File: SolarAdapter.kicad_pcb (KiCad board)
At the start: 2 copper layers, 32.4 x 18 mm, 7 parts, among them J1 Conn_02x03_Odd_Even, J2 USB_A

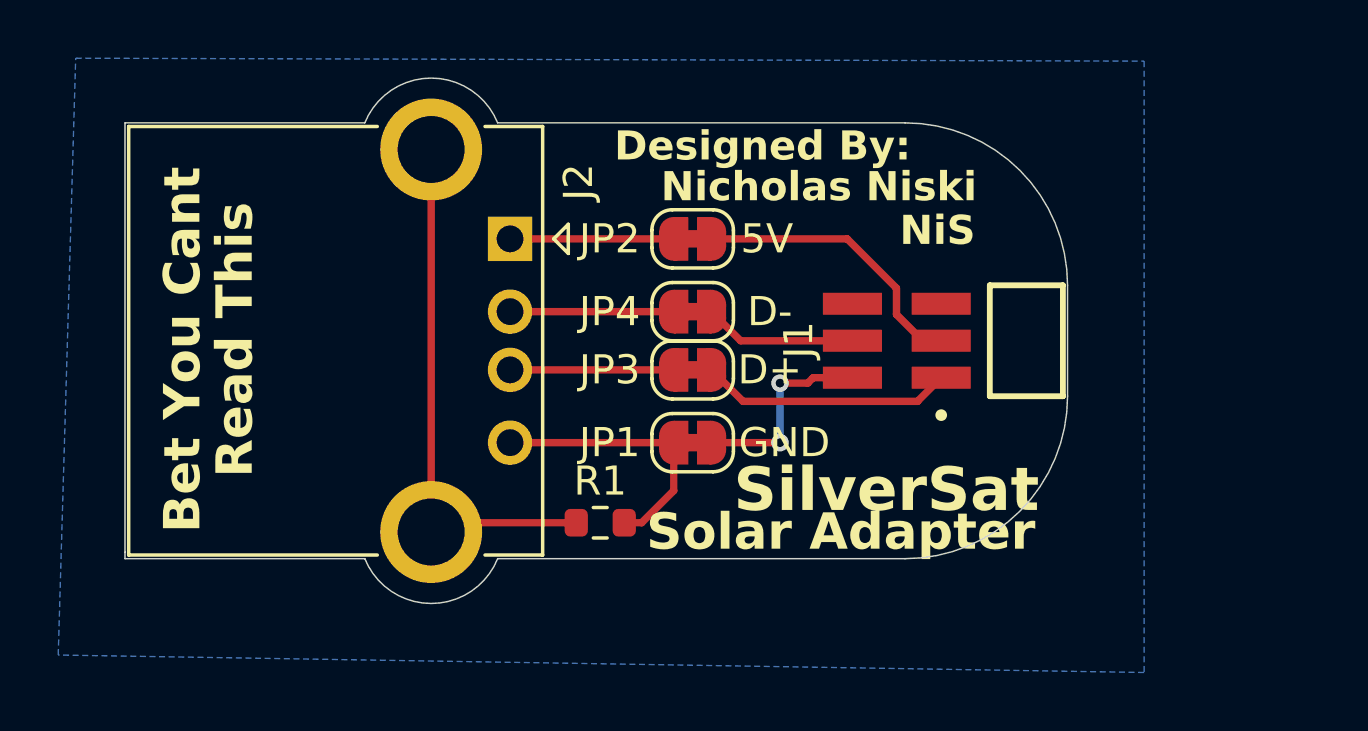
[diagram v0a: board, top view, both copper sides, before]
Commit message: Solar Adapter 1.1
Release Notes:
1. Added MPNs to parts(whoops)
2. Beefed up power traces to allow for higher current draws
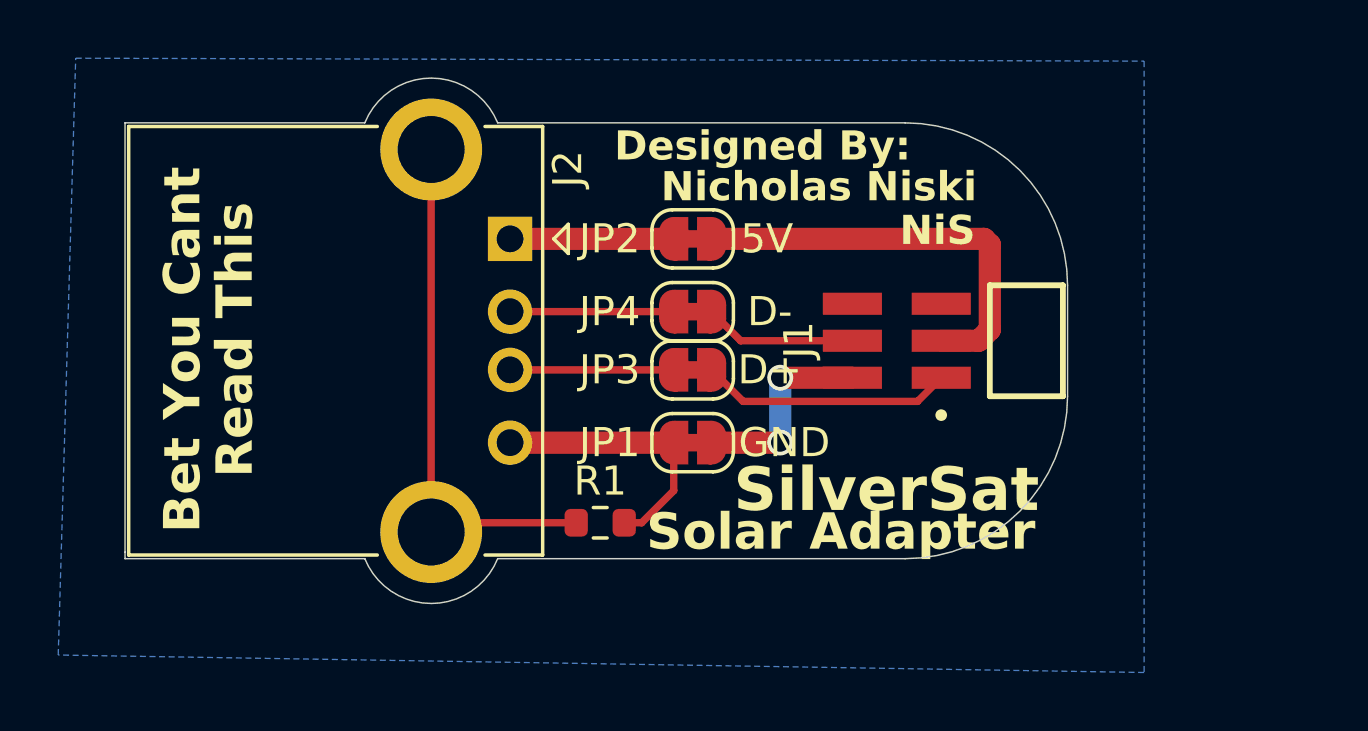
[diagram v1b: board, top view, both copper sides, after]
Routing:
- net /CVBUS: track 9.87 -> 15.0 mm
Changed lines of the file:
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@@
 		(sheetfile "SolarAdapter.kicad_sch")
 		(zone_connect 1)
-		(attr exclude_from_pos_files)
+		(attr exclude_from_pos_files exclude_from_bom)
 		(net_tie_pad_groups "1, 2")
 		(fp_poly
@@
 		(sheetfile "SolarAdapter.kicad_sch")
 		(zone_connect 1)
-		(attr exclude_from_pos_files)
+		(attr exclude_from_pos_files exclude_from_bom)
 		(net_tie_pad_groups "1, 2")
 		(fp_poly
@@
 		(tags "USB-A receptacle horizontal through-hole")
 		(property "Reference" "J2"
-			(at -1.95 -2.35 90)
+			(at -2.405 -1.98 90)
 			(layer "F.SilkS")
 			(effects
@@
 				(font
 					(size 1.27 1.27)
+				)
+			)
+		)
+		(property "MPN" "6364372-2"
+			(at 0 0 -90)
+			(unlocked yes)
+			(layer "F.Fab")
+			(hide yes)
+			(effects
+				(font
+					(size 1 1)
+					(thickness 0.15)
 				)
 			)
@@
 		(sheetfile "SolarAdapter.kicad_sch")
 		(zone_connect 1)
-		(attr exclude_from_pos_files)
+		(attr exclude_from_pos_files exclude_from_bom)
 		(net_tie_pad_groups "1, 2")
 		(fp_poly
@@
 			)
 		)
+		(property "MPN" "FTSH-103-04-L-DH"
+			(at 0 0 -90)
+			(unlocked yes)
+			(layer "F.Fab")
+			(hide yes)
+			(effects
+				(font
+					(size 1 1)
+					(thickness 0.15)
+				)
+			)
+		)
 		(property ki_fp_filters "Connector*:*_2x??_*")
 		(sheetname "Root")
@@
 			)
 		)
+		(property "MPN" "ERJ-PA3F1004V"
+			(at 0 0 0)
+			(unlocked yes)
+			(layer "F.Fab")
+			(hide yes)
+			(effects
+				(font
+					(size 1 1)
+					(thickness 0.15)
+				)
+			)
+		)
 		(property ki_fp_filters "R_*")
 		(sheetname "Root")
@@
 		(sheetfile "SolarAdapter.kicad_sch")
 		(zone_connect 1)
-		(attr exclude_from_pos_files)
+		(attr exclude_from_pos_files exclude_from_bom)
 		(net_tie_pad_groups "1, 2")
 		(fp_poly
@@
 		(start 103.7275 78.5)
 		(end 109.35 78.5)
-		(width 0.254)
+		(width 0.762)
 		(layer "F.Cu")
 		(net 3)
@@
 	)
 	(segment
-		(start 103.7275 85.5)
-		(end 109.35 85.5)
+		(start 107.65 88.25125)
+		(end 108.24875 88.25125)
 		(width 0.254)
 		(layer "F.Cu")
@@
 	)
 	(segment
-		(start 107.65 88.25125)
-		(end 108.24875 88.25125)
-		(width 0.254)
+		(start 103.7275 85.5)
+		(end 109.35 85.5)
+		(width 0.762)
 		(layer "F.Cu")
 		(net 4)
@@
 	)
 	(segment
-		(start 113 83.455)
-		(end 113.955 83.455)
-		(width 0.254)
+		(start 113.0025 85.5)
+		(end 113.0075 85.495)
+		(width 0.762)
 		(layer "F.Cu")
 		(net 6)
 	)
 	(segment
-		(start 114.14 83.27)
+		(start 113.0075 83.27)
 		(end 115.4875 83.27)
-		(width 0.254)
+		(width 0.762)
 		(layer "F.Cu")
 		(net 6)
@@
 	(segment
 		(start 110.65 85.5)
-		(end 113 85.5)
-		(width 0.254)
+		(end 113.0025 85.5)
+		(width 0.762)
 		(layer "F.Cu")
 		(net 6)
 	)
-	(segment
-		(start 113.955 83.455)
-		(end 114.14 83.27)
-		(width 0.254)
-		(layer "F.Cu")
-		(net 6)
-	)
 	(via
-		(at 113 85.5)
-		(size 0.6)
-		(drill 0.3)
+		(at 113.0075 83.27)
+		(size 0.889)
+		(drill 0.635)
 		(layers "F.Cu" "B.Cu")
 		(net 6)
 	)
 	(via
-		(at 113 83.455)
-		(size 0.6)
-		(drill 0.3)
+		(at 113.0075 85.495)
+		(size 0.889)
+		(drill 0.635)
 		(layers "F.Cu" "B.Cu")
 		(net 6)
 	)
 	(segment
-		(start 113 85.5)
-		(end 113 83.455)
-		(width 0.254)
+		(start 113.0075 85.495)
+		(end 113.0075 83.27)
+		(width 0.762)
 		(layer "B.Cu")
 		(net 6)
 	)
 	(segment
-		(start 115.3065 78.5)
-		(end 117 80.1935)
-		(width 0.254)
+		(start 120.2075 81.617)
+		(end 119.8245 82)
+		(width 0.762)
 		(layer "F.Cu")
 		(net 7)
 	)
 	(segment
-		(start 117 81.0975)
-		(end 117.9025 82)
-		(width 0.254)
+		(start 120.2075 78.695)
+		(end 120.2075 81.617)
+		(width 0.762)
 		(layer "F.Cu")
 		(net 7)
@@
 	)
 	(segment
-		(start 117 80.1935)
-		(end 117 81.0975)
-		(width 0.254)
+		(start 120.0125 78.5)
+		(end 120.2075 78.695)
+		(width 0.762)
 		(layer "F.Cu")
 		(net 7)
 	)
 	(segment
-		(start 110.65 78.5)
-		(end 115.3065 78.5)
-		(width 0.254)
+		(start 119.8245 82)
+		(end 118.5375 82)
+		(width 0.762)
 		(layer "F.Cu")
 		(net 7)
+	)
+	(segment
+		(start 110.65 78.5)
+		(end 120.0125 78.5)
+		(width 0.762)
+		(layer "F.Cu")
+		(net 7)

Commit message: Solar Adapter 1.1.1
Patch Notes:
1. Original connector was too short, so it was replaced with a longer connector
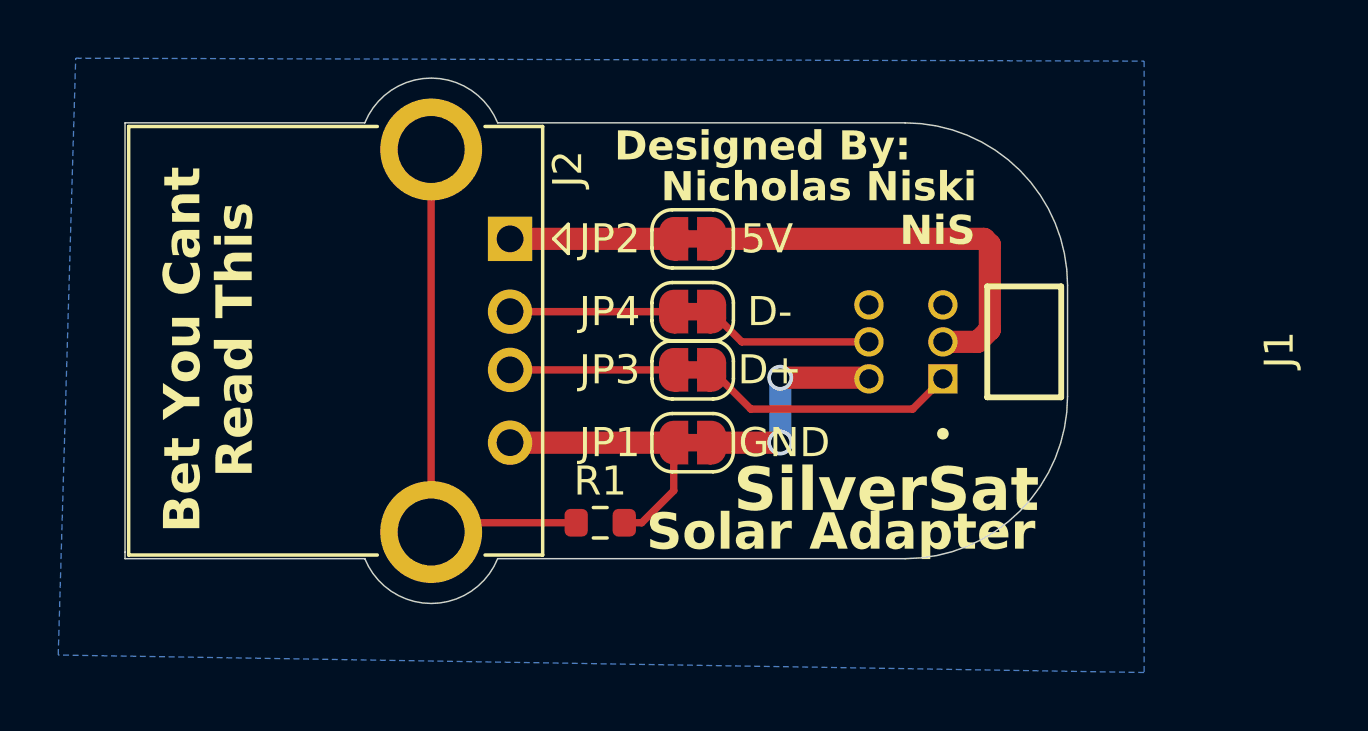
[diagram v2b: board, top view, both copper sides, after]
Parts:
- J1: footprint SolarAdapter:SAMTEC_FTSH-103-04-L-DH -> SolarAdapter:SAMTEC_TMS-103-01-L-D-RA
- moved J1 0.32 mm to (117.3, 82.0)
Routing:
- net /CVBUS: track 15.0 -> 14.3 mm
- net GND1: track 7.06 -> 7.65 mm
- net /CD-: track 5.25 -> 5.84 mm
